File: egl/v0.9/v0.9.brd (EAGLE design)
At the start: 100 x 105 mm, 57 parts, among them IC1 74HC125N, IC2 TINY25, IC3 ATTINY2313, Q2 12Mhz, X2 USBB-G

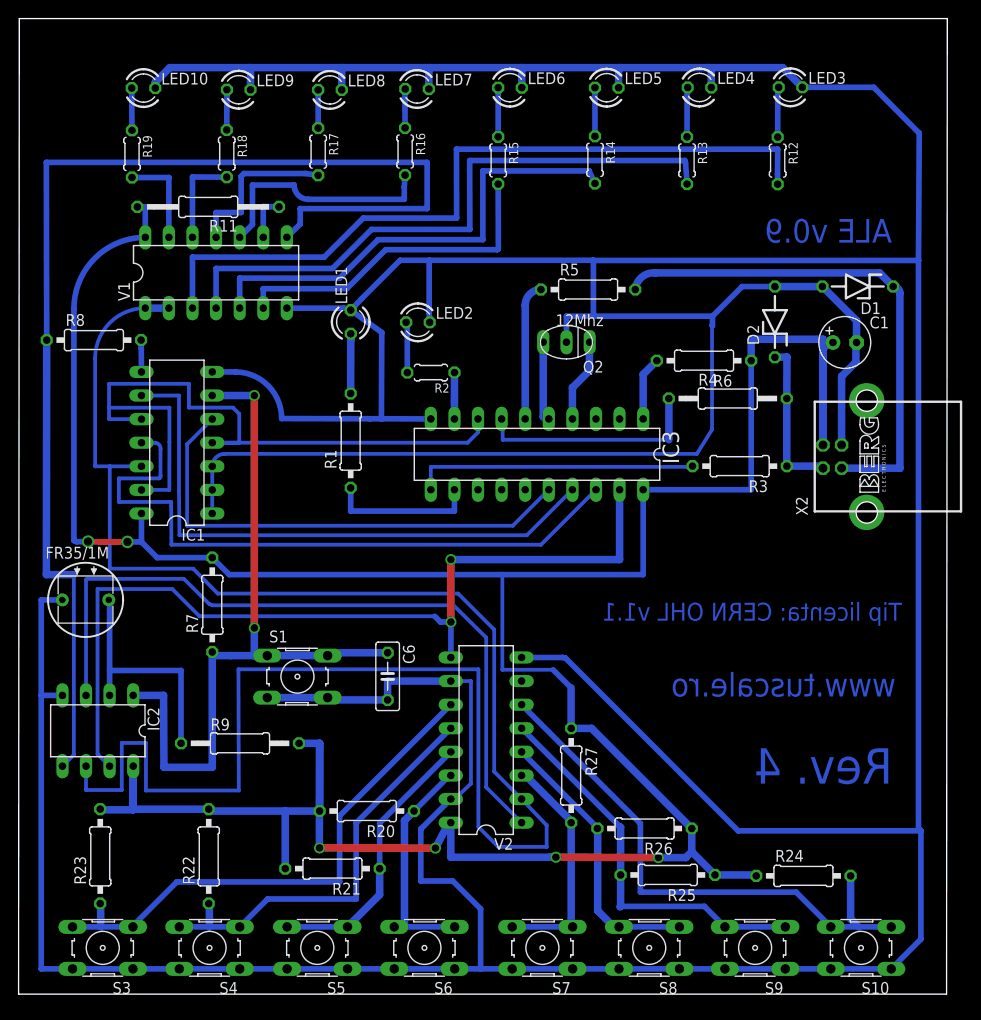
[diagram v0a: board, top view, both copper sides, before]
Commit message: [work on eagle] Made the board a perfect fit in a 100x100mm square and made it ready for manufacturer production by grouping objects in appropriate layers.
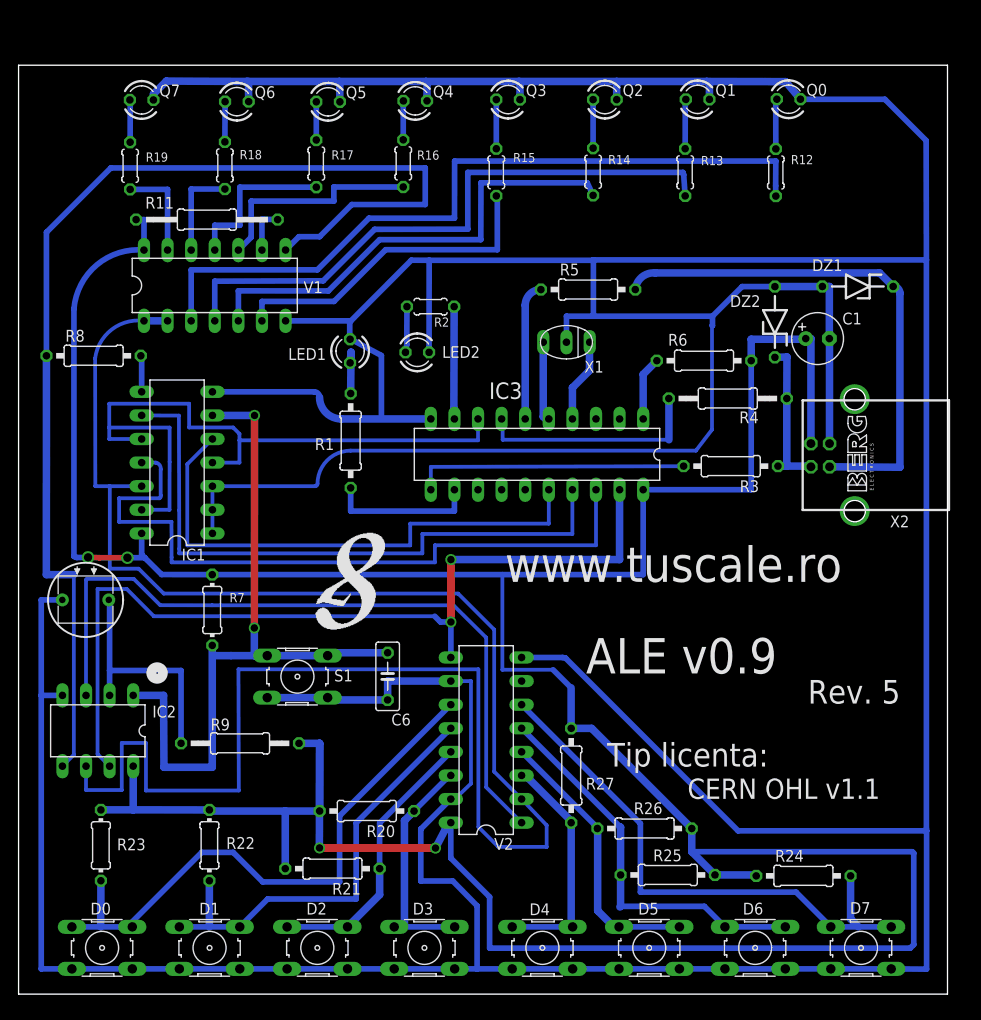
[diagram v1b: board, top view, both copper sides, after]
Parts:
- removed LED10, LED3, LED4, LED5, LED6, LED7, LED8, LED9: Verde, led:LED3MM
- removed S3, S4, S5: TACT-64N, switch-omron:B3F-10XX
- added D0: TACT-64N, switch-omron:B3F-10XX
- added DZ1, DZ2: 3v3, diode:ZDIO-7.5
- added Q0, Q1, Q3, Q4, Q5, Q6, Q7: Verde, led:LED3MM
- added X1: 12Mhz, murata-resonators:CSTLS_X
- D1, D2: value 3v3 -> TACT-64N; device diode:ZDIO-7.5 -> switch-omron:B3F-10XX
- Q2: value 12Mhz -> Verde; device murata-resonators:CSTLS_X -> led:LED3MM
- R22, R23, R7: device rcl:0207/10 -> rcl:0204/7
- moved D1 99.7 mm to (20.6, 4.98)
- moved D2 83.5 mm to (32.2, 4.98), turned to 180 degrees
- moved Q2 26.4 mm to (63.1, 96.3), turned to 0 degrees
- moved R2 7.10 mm to (44.4, 74.0)
- moved LED2 3.23 mm to (42.9, 69.1)
- moved LED1 3.13 mm to (35.7, 69.2)
- moved C1 2.96 mm to (86.0, 70.6)
- moved IC1 2.14 mm to (17.1, 57.2)
- moved R8 1.69 mm to (8.08, 68.7)
- moved R11 1.38 mm to (20.3, 83.4)
- moved V1 1.38 mm to (21.1, 76.3)
- moved X2 1.31 mm to (90.0, 58.0)
- moved R12 1.30 mm to (81.5, 88.5)
- moved R15 1.30 mm to (51.4, 88.5)
- moved R17 1.30 mm to (32.0, 89.4)
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- renumbered S10 to D7, S6 to D3, S7 to D4, S8 to D5, S9 to D6
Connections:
- net GND: now also D0.1, D0.2, D1.1, D1.2, D2.1, D2.2, DZ1.A, DZ2.A, Q0.K, Q1.K, Q2.K, Q3.K, Q4.K, Q5.K, Q6.K, Q7.K, X1.2; no longer D1.A, D2.A, LED10.K, LED3.K, LED4.K, LED5.K, LED6.K, LED7.K, LED8.K, LED9.K, Q2.2, S3.1, S3.2, S4.1, S4.2, S5.1, S5.2
- net N$11: now also D0.3, D0.4; no longer S3.3, S3.4
- net N$12: now also Q0.A; no longer LED3.A
- net N$17: now also DZ2.C; no longer D2.C
- net N$18: now also X1.1; no longer Q2.1
- net N$19: now also DZ1.C; no longer D1.C
- net N$20: now also X1.3; no longer Q2.3
- net N$21: now also Q1.A; no longer LED4.A
- net N$22: now also Q2.A; no longer LED5.A
- net N$23: now also Q3.A; no longer LED6.A
- net N$24: now also Q4.A; no longer LED7.A
- net N$25: now also Q5.A; no longer LED8.A
- net N$26: now also Q6.A; no longer LED9.A
- net N$27: now also Q7.A; no longer LED10.A
- net N$36: now also D1.3, D1.4; no longer S4.3, S4.4
- net N$37: now also D2.3, D2.4; no longer S5.3, S5.4
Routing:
- net VCC_USB: track 330.3 -> 377.3 mm, vias 6 -> 4
- net GND: track 686.3 -> 694.4 mm
- net N$10: track 4.99 -> 12.1 mm
- net UCMOSI: track 131.8 -> 125.6 mm
- net N$11: track 57.4 -> 63.1 mm
- net N$5: track 70.8 -> 75.9 mm
- net N$2: track 63.4 -> 68.0 mm
- net N$1: track 53.1 -> 57.5 mm
- net 125_EN: track 79.0 -> 76.5 mm
- net N$36: track 45.5 -> 47.8 mm
- net N$32: track 25.8 -> 23.7 mm
- net N$19: track 55.2 -> 56.4 mm
- net UCMISO: track 200.9 -> 199.9 mm
- net N$29: track 66.5 -> 65.6 mm
- net N$14: track 6.43 -> 5.60 mm
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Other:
- board size 100 x 105 mm -> 100 x 100 mm
- board text added: "CERN OHL v1.1"
- board text added: "Rev. 5"
- board text added: "Tip licenta:"
- board text removed: "Rev. 4"
- board text removed: "Tip licenta: CERN OHL v1.1"
